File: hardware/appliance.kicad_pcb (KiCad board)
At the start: 2 copper layers, 657 parts, among them J101 3.3V RAIL TEST, J102 CONTROL BOUNDARY, J1201 RECOVERY USB, J1202 3.3V DEBUG UART, J1711 ED555/2DS, J1712 87898-0204, J2002 1042240820, J201 SWD / recovery, J202 WDT RUN jumper, Q1201 MMBT3904,215, Q1601 MMBT3904,215, Q1701 100V, Q1702 100V, Q1703 100V, Q1704 100V, Q1705 150V, Q1707 20 V, Q1901 AO3400A, Q2001 MMBT3904,215, Q301 MMBT3904,215, Q302 MMBT3904,215, Q303 MMBT3904,215, Q501 MMBT3904,215, Q801 MMBT3904,215, Q802 MMBT3904,215, SW201 RESET, SW801 PROCESSOR RECOVERY, SW802 PROCESSOR / PMIC RESET, T1702 30uH, U1001 TCS4525_WT, U1101 IS21TF16G-JCLI, U1201 SN74LVC1G125DCKR, U1202 SN74LVC1G125DCKR, U1203 SN74LVC1G125DCKR, U1301 RTL8125BG-CG, U1302 93LC46BT-I/SN, U1501 SN74LVC1G125DCKR, U1502 TPS22965DSGR, U1503 SY8089AAAC, U1504 TPS3808G33DBVR, U1505 TPS3808G01DBVR, U1601 SN74LVC1G07DCKR, U1602 SN74LVC1G07DCKR, U1603 SN74LVC1G07DCKR, U1604 TMUXHS4212IRKSR, U1701 TPS2373-3RGWR, U1702 LM51551QDSSRQ1, U1703 FOD817AS, U1704 TL431LIAIDBZR, U1801 TLP293(GB-TPL,E), U1802 TLP293(GB-TPL,E), U1803 TLP293(GB-TPL,E), U1901 TPS54620RHLR, U1902 TPS259474LRPWR, U1903 TPS3808G01DBVR, U1904 SN74LVC1G04DCKR, U2001 TMUXHS4212IRKSR, U2002 TS3USB221ARSER, U2003 SN74LVC1G08DCKR, U201 STM32G0B1CCT6, U202 TPS3828-33DBVR, U401 TPS62177DQCR, U501 RK809-5, U601 MP2143DJ-LF-Z, U602 SN74LVC1G17DBVR, U902 SY8089AAAC, Y1101 SiT8008BI-21-18E-24.000000, Y1301 25MHz, 18pF

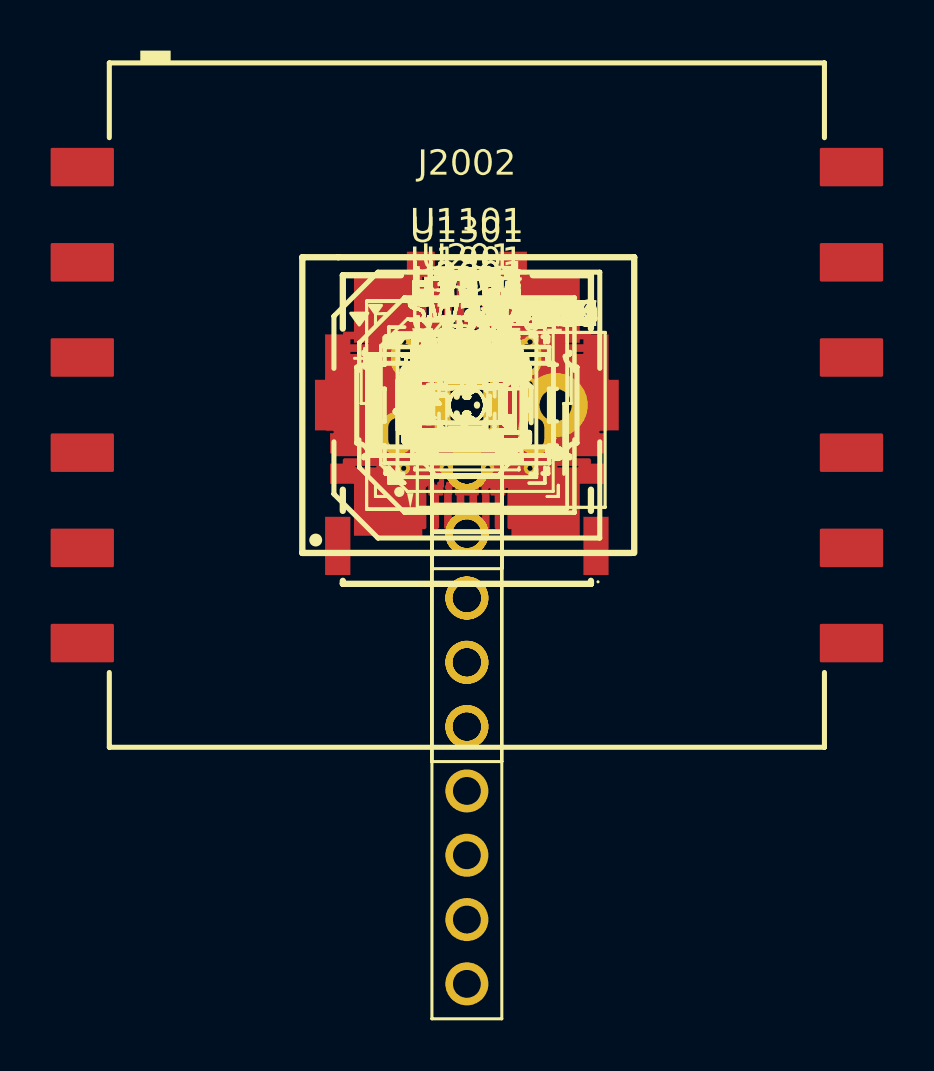
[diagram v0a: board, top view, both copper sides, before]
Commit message: Audit appliance footprints, models and native schematic PCB synchronization
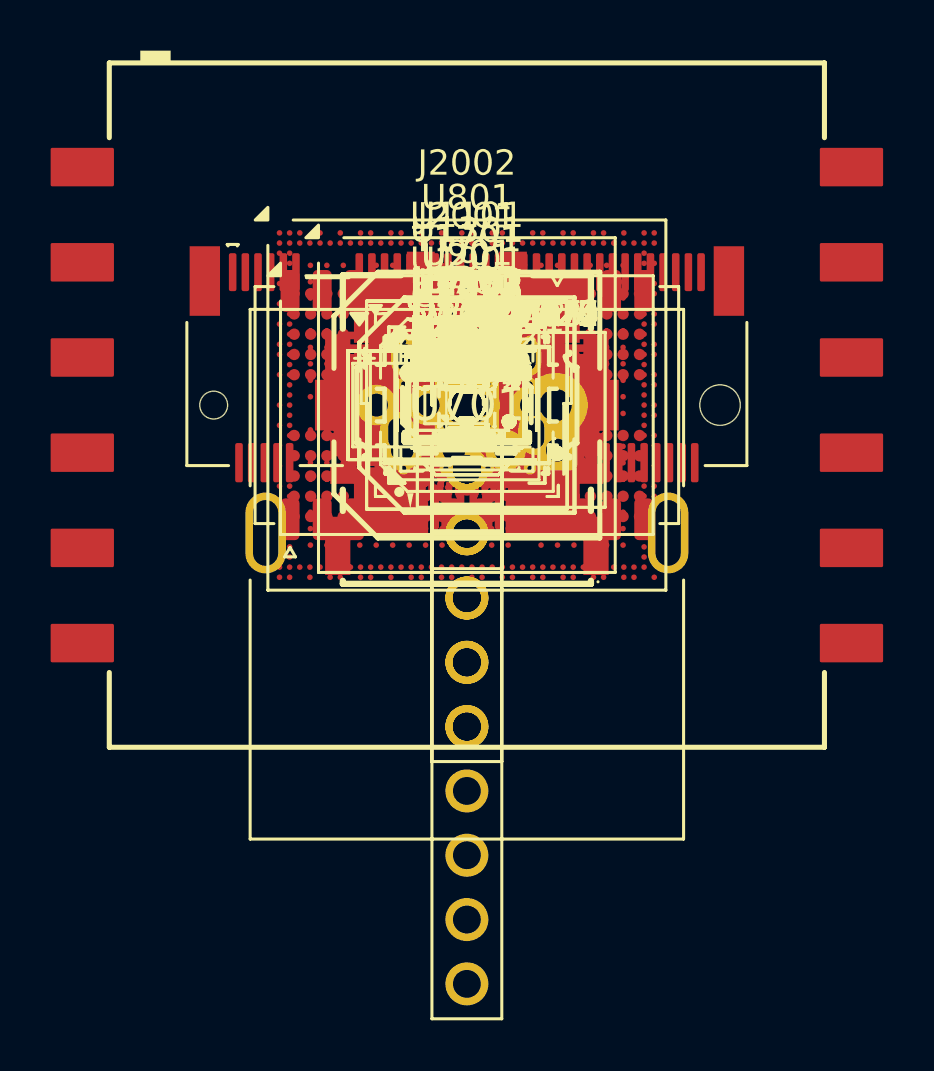
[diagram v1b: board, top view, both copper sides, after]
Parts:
- added J1701: 2.5GbE + PoE, Appliance:Sierra_RJE491881401_1x08-1MP_P1.02mm, F.Cu at (0.00, 0.00)
- added J2001: MDT420B01411, Appliance:Sierra_MDT420B01411_2x38-1MP_P0.5mm, F.Cu at (0.00, 0.00)
- added T1701: HX4110NLT, Appliance:Sierra_HX4110NL_2x12_P1.27mm, F.Cu at (0.00, 0.00)
- added U701: TPS56837RPAR, Appliance:Texas_RPA0010A_TPS56837, F.Cu at (0.00, 0.00)
- added U801: RK3566, Appliance:Sierra_RK3566_BGA565, F.Cu at (0.00, 0.00)
- added U901: MT53E512M32D1ZW-046 WT:B, Appliance:Sierra_Micron_ZW_TFBGA200, F.Cu at (0.00, 0.00)
- C1001, C1101, C1503, C1505, C1507, C1905, C1906, C203, C401, C537, C542, C543, C544, C703, C704, C823, C830, C835, C841, C902, C903, C905, C909, C914, C915, C916, C934, C935, C936, C955, C958: footprint Capacitor_SMD:C_1206_3216Metric -> Capacitor_SMD:C_1206_3216Metric_Pad1.33x1.80mm_HandSolder
- C1002, C1005, C1006, C1102, C1103, C1104, C1105, C1201, C1202, C1203, C1204, C1205, C1206, C1207, C1208, C1209, C1210, C1211, C1212, C1301, C1302, C1303, C1401, C1402, C1403, C1404, C1405, C1406, C1407, C1408, C1409, C1410, C1411, C1412, C1420, C1421, C1422, C1423, C1424, C1425, C1426, C1427, C1428, C1429, C1430, C1431, C1432, C1433, C1434, C1441, C1442, C1443, C1444, C1501, C1502, C1504, C1508, C1509, C1605, C1606, C1607, C1608, C1620, C1621, C1622, C1623, C1624, C1625, C1626, C1627, C1628, C1629, C1630, C1631, C1632, C1633, C1640, C1641, C1642, C1643, C1644, C1716, C1718, C1801, C1802, C1803, C1851, C1852, C1853, C1854, C1861, C1862, C1863, C1864, C1901, C1907, C1908, C1909, C1910, C1911, C1912, C1913, C1914, C2001, C2002, C2003, C2004, C2005, C201, C202, C2021, C2022, C2023, C2024, C2031, C2032, C2033, C2034, C2035, C2036, C2037, C2038, C204, C2041, C2042, C2043, C2044, C2045, C205, C513, C514, C515, C517, C518, C520, C521, C522, C523, C525, C526, C527, C528, C529, C530, C531, C532, C535, C536, C538, C545, C546, C547, C604, C701, C702, C705, C801, C802, C803, C804, C805, C806, C807, C808, C809, C810, C811, C812, C813, C814, C815, C816, C817, C818, C819, C820, C821, C825, C826, C827, C828, C832, C833, C837, C838, C839, C840, C842, C843, C844, C845, C846, C906, C907, C908, C910, C911, C912, C917, C918, C919, C920, C921, C922, C923, C924, C925, C926, C927, C928, C929, C930, C931, C932, C937, C938, C939, C940, C941, C942, C943, C944, C945, C946, C947, C948, C949, C950, C951, C952, C953, C954, C959, C960: footprint Capacitor_SMD:C_0603_1608Metric -> Capacitor_SMD:C_0603_1608Metric_Pad1.08x0.95mm_HandSolder
- C1003, C1004, C1007, C1008, C1009, C1506, C1902, C1903, C1904, C402, C403, C501, C502, C503, C504, C505, C506, C507, C508, C509, C510, C511, C512, C516, C519, C524, C533, C541, C601, C602, C603, C706, C707, C822, C824, C829, C831, C834, C836, C901, C913, C933, C956, C957: footprint Capacitor_SMD:C_1210_3225Metric -> Capacitor_SMD:C_1210_3225Metric_Pad1.33x2.70mm_HandSolder
- C1601, C1602, C1603, C1604: footprint Capacitor_SMD:C_0201_0603Metric -> Capacitor_SMD:C_0201_0603Metric_Pad0.64x0.40mm_HandSolder
- C1707, C1708, C1709, C1710, C1711, C1712, C1734, C1737: footprint PoE:TI_0603_1 -> Capacitor_SMD:C_0603_1608Metric_Pad1.08x0.95mm_HandSolder
- C1719: footprint Capacitor_SMD:C_0805_2012Metric -> Capacitor_SMD:C_0805_2012Metric_Pad1.18x1.45mm_HandSolder
- C1720: footprint PoE:TI_1812_254_1 -> Capacitor_SMD:C_1812_4532Metric_Pad1.57x3.40mm_HandSolder; moved to F.Cu
- C1721, C1726, C1731, C1732, C1740: footprint PoE:TI_0805_HV -> Capacitor_SMD:C_0805_2012Metric_Pad1.18x1.45mm_HandSolder
- C1722, C1723, C1724, C1725: footprint PoE:TI_1210_270 -> Capacitor_SMD:C_1210_3225Metric_Pad1.33x2.70mm_HandSolder
- C1728, C1729, C1730: footprint PoE:TI_1210_280 -> Capacitor_SMD:C_1210_3225Metric_Pad1.33x2.70mm_HandSolder; moved to F.Cu
- C1733, C1738: footprint PoE:TI_0603L -> Capacitor_SMD:C_0603_1608Metric_Pad1.08x0.95mm_HandSolder
- C1735, C1744, C1745: footprint PoE:TI_0603L_1 -> Capacitor_SMD:C_0603_1608Metric_Pad1.08x0.95mm_HandSolder
- C1736: footprint PoE:TI_1812_254 -> Capacitor_SMD:C_1812_4532Metric_Pad1.57x3.40mm_HandSolder; moved to F.Cu
- C1739: footprint PoE:TI_0603_3 -> Capacitor_SMD:C_0603_1608Metric_Pad1.08x0.95mm_HandSolder
- C1741, C1743: footprint PoE:TI_0603 -> Capacitor_SMD:C_0603_1608Metric_Pad1.08x0.95mm_HandSolder
- C1746: footprint PoE:TI_0805L -> Capacitor_SMD:C_0805_2012Metric_Pad1.18x1.45mm_HandSolder
- C1865: footprint Capacitor_SMD:C_1808_4520Metric -> Capacitor_SMD:C_1808_4520Metric_Pad1.72x2.30mm_HandSolder
- D1201: footprint Appliance:SOT-9X3-3_L1.0-W0.8-P0.35-LS1.0-BR -> Package_TO_SOT_SMD:Texas_DRT-3
- D1701, D1702, D1703, D1704, D1706, D1707, D1708, D1709: footprint PoE:TI_SMB -> Diode_SMD:D_SMB_Handsoldering
- D1705: footprint PoE:TI_SMB_1 -> Diode_SMD:D_SMB_Handsoldering
- D1714: footprint PoE:TI_SMA -> Diode_SMD:D_SMA_Handsoldering; moved to F.Cu
- D1715, D1717: footprint PoE:TI_SOD-123 -> Diode_SMD:D_SOD-123
- D1716: footprint PoE:TI_WL-SMCW_YELLOW -> LED_SMD:LED_0603_1608Metric_Pad1.05x0.95mm_HandSolder
- D1718: footprint PoE:TI_PowerDI5 -> Appliance:Diodes_PowerDI-5_3Pin_Derived; moved to F.Cu
- D1719: footprint PoE:TI_SOD-123_1 -> Diode_SMD:D_SOD-123; moved to F.Cu
- D1721: footprint PoE:TI_SOT-23 -> Package_TO_SOT_SMD:SOT-23_Handsoldering
- D1851, D1852, D2001: footprint Appliance:USON-10_L2.5-W1.0-P0.50-BL -> Package_SON:USON-10_2.5x1.0mm_P0.5mm
- FB1301, FB1302, FB1401, FB1402, FB1403, FB1404, FB801, FB802: footprint Inductor_SMD:L_0603_1608Metric -> Inductor_SMD:L_0603_1608Metric_Pad1.05x0.95mm_HandSolder
- FB1303, FB1304: footprint Inductor_SMD:L_0805_2012Metric -> Inductor_SMD:L_0805_2012Metric_Pad1.05x1.20mm_HandSolder
- L1701, L1703: footprint PoE:TI_WE-CBF_0603 -> Inductor_SMD:L_0603_1608Metric_Pad1.05x0.95mm_HandSolder
- L1707: footprint PoE:TI_XFL4020 -> Inductor_SMD:L_Coilcraft_XxL4020
- L1708: footprint PoE:TI_XAL5030 -> Inductor_SMD:L_Coilcraft_XAL5030-XXX
- Q1201, Q1601, Q1901, Q2001, Q301, Q302, Q303, Q501, Q801, Q802: footprint Package_TO_SOT_SMD:SOT-23 -> Package_TO_SOT_SMD:SOT-23_Handsoldering
- Q1701, Q1702, Q1703, Q1704: footprint PoE:TI_SSOT-3 -> Package_TO_SOT_SMD:SuperSOT-3
- Q1707: footprint PoE:TI_SOT-23_1 -> Package_TO_SOT_SMD:SOT-23_Handsoldering
- R1001, R1101, R1102, R1103, R1104, R1105, R1106, R1201, R1202, R1203, R1204, R1205, R1206, R1207, R1208, R1209, R1210, R1211, R1301, R1302, R1303, R1304, R1305, R1306, R1307, R1401, R1402, R1403, R1411, R1412, R1413, R1414, R1501, R1502, R1503, R1504, R1505, R1506, R1507, R1508, R1509, R1510, R1602, R1603, R1604, R1605, R1606, R1723, R1724, R1727, R1732, R1801, R1802, R1803, R1811, R1812, R1813, R1861, R1862, R1863, R1864, R1901, R1902, R1903, R1904, R1905, R1906, R1907, R1911, R1912, R1913, R1914, R1915, R1916, R1917, R1918, R1921, R1922, R1923, R1925, R1926, R2001, R2002, R2003, R201, R2011, R2012, R2013, R2014, R2015, R2016, R2017, R2018, R202, R2021, R2022, R2023, R2024, R203, R301, R302, R303, R304, R305, R306, R307, R308, R401, R501, R502, R503, R504, R505, R506, R507, R508, R509, R510, R511, R512, R601, R602, R603, R604, R605, R606, R701, R702, R703, R704, R705, R706, R801, R802, R803, R804, R805, R901, R902, R903, R904, R905, R906, R907, R908: footprint Resistor_SMD:R_0603_1608Metric -> Resistor_SMD:R_0603_1608Metric_Pad0.98x0.95mm_HandSolder
- R1709, R1710, R1711, R1712, R1713, R1714, R1715, R1716, R1737, R1741, R1744, R1753, R1760, R1763: footprint PoE:TI_0603_2 -> Resistor_SMD:R_0603_1608Metric_Pad0.98x0.95mm_HandSolder
- R1730: footprint Resistor_SMD:R_2010_5025Metric -> Resistor_SMD:R_2010_5025Metric_Pad1.40x2.65mm_HandSolder
- R1733: footprint PoE:TI_1206 -> Resistor_SMD:R_1206_3216Metric_Pad1.30x1.75mm_HandSolder; moved to F.Cu
- R1734, R1735, R1740, R1742, R1743, R1745, R1746, R1757: footprint PoE:TI_0603 -> Resistor_SMD:R_0603_1608Metric_Pad0.98x0.95mm_HandSolder
- R1736: footprint PoE:TI_2010L -> Resistor_SMD:R_2010_5025Metric_Pad1.40x2.65mm_HandSolder; moved to F.Cu
- R1738: footprint PoE:TI_2010 -> Resistor_SMD:R_2010_5025Metric_Pad1.40x2.65mm_HandSolder
- R1739: footprint PoE:TI_0805_HV_1 -> Resistor_SMD:R_0805_2012Metric_Pad1.20x1.40mm_HandSolder
- R1747, R1748: footprint PoE:TI_2512 -> Resistor_SMD:R_2512_6332Metric_Pad1.40x3.35mm_HandSolder; moved to F.Cu
- R1754, R1762: footprint PoE:TI_0603L -> Resistor_SMD:R_0603_1608Metric_Pad0.98x0.95mm_HandSolder
- R1755, R1756, R1759, R1761: footprint PoE:TI_0603L_2 -> Resistor_SMD:R_0603_1608Metric_Pad0.98x0.95mm_HandSolder
- R1924: footprint Resistor_SMD:R_1206_3216Metric -> Resistor_SMD:R_1206_3216Metric_Pad1.30x1.75mm_HandSolder
- U1101: footprint Appliance:VFBGA-153_L13.0-W11.5-P0.50-BL_ISSI_IS2XES0XG-XXXX -> Package_BGA:LFBGA-153_11.5x13mm_Layout14x14_P0.5mm
- U1502: footprint Appliance:UDFN-8_L2.0-W2.0-P0.50-TL-EP -> Package_SON:Texas_DSG0008A_WSON-8-1EP_2x2mm_P0.5mm_EP0.9x1.6mm
- U1503, U202, U602, U902: footprint Package_TO_SOT_SMD:SOT-23-5 -> Package_TO_SOT_SMD:SOT-23-5_HandSoldering
- U1504, U1505, U1903: footprint Package_TO_SOT_SMD:SOT-23-6 -> Package_TO_SOT_SMD:SOT-23-6_Handsoldering
- U1604, U2001: footprint Appliance:DHVQFN-20_L4.5-W2.5-P0.50-BL-EP -> Package_DFN_QFN:DHVQFN-20-1EP_2.5x4.5mm_P0.5mm_EP1x3mm
- U1701: footprint PoE:TI_RGW0020B -> Package_DFN_QFN:Texas_RGW0020A_VQFN-20-1EP_5x5mm_P0.65mm_EP3.15x3.15mm
- U1702: footprint PoE:TI_DSS0012C -> Package_SON:WSON-12-1EP_3x2mm_P0.5mm_EP1x2.65; moved to F.Cu
- U1704: footprint PoE:TI_DBZ0003A_M -> Package_TO_SOT_SMD:SOT-23_Handsoldering
- U601: footprint Package_TO_SOT_SMD:TSOT-23-8 -> Package_TO_SOT_SMD:TSOT-23-8_HandSoldering
- Y1301: footprint Crystal:Crystal_SMD_3225-4Pin_3.2x2.5mm -> Crystal:Crystal_SMD_TXC_7M-4Pin_3.2x2.5mm_HandSoldering
